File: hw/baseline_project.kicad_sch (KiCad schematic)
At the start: 20 parts, among them J101 EXT_3V3, Q101 IRLD024PBF, SW101 UP, SW102 DOWN, SW103 LEFT, SW104 RIGHT, SW105 MODE, U101 EK-TM4C123GXL, U102 ESP8266-1, U103 Adafruit ST7735R

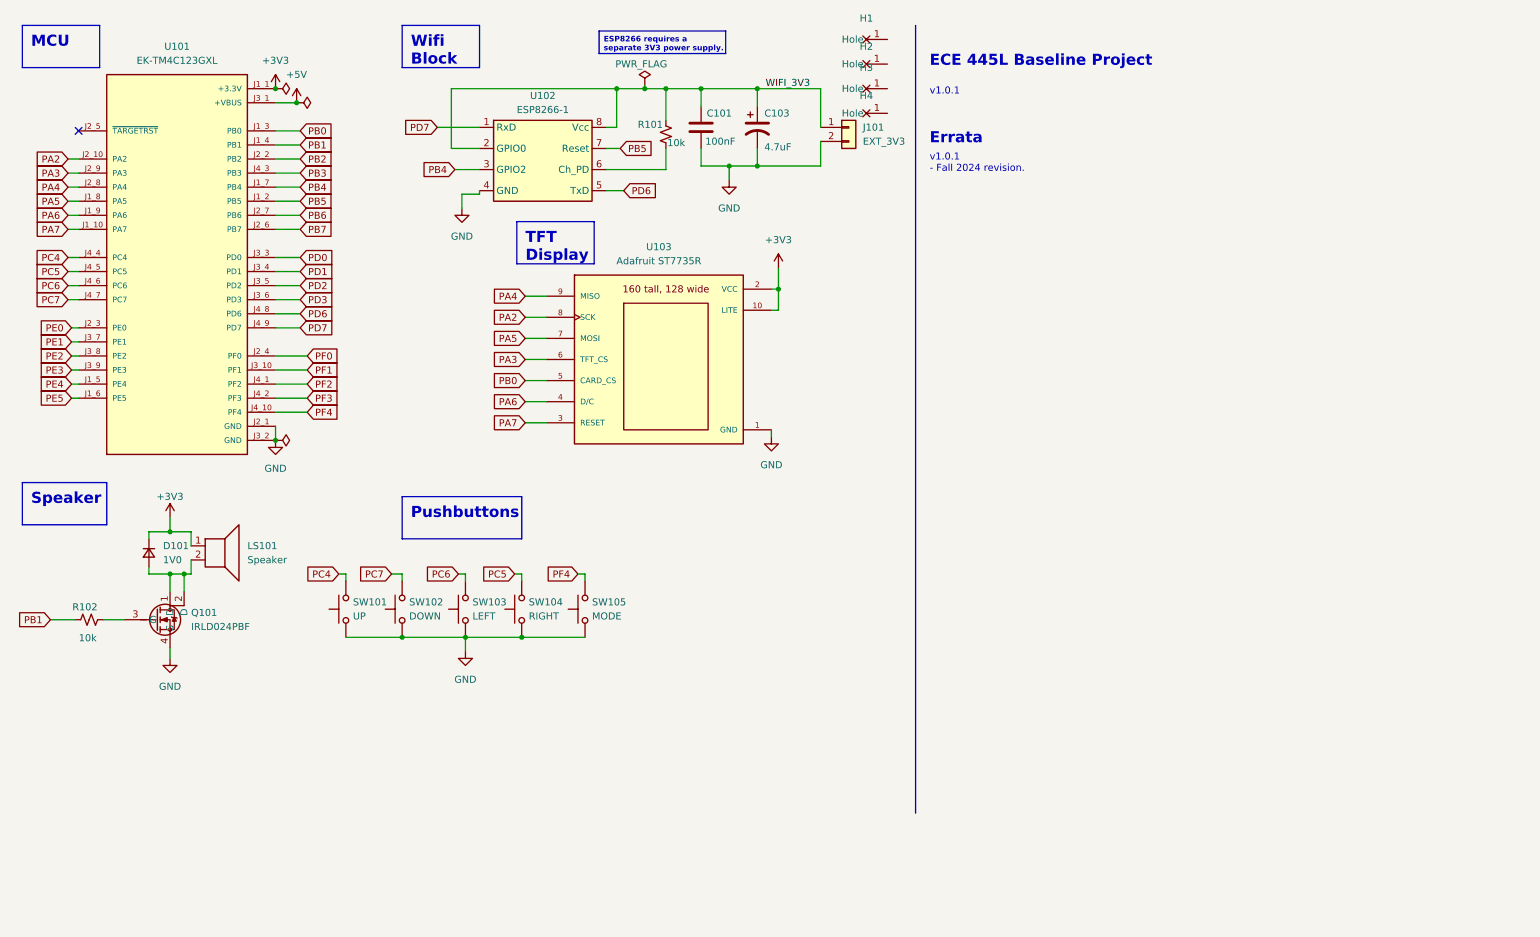
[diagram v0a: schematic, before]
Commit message: worked on actual timer funcnality
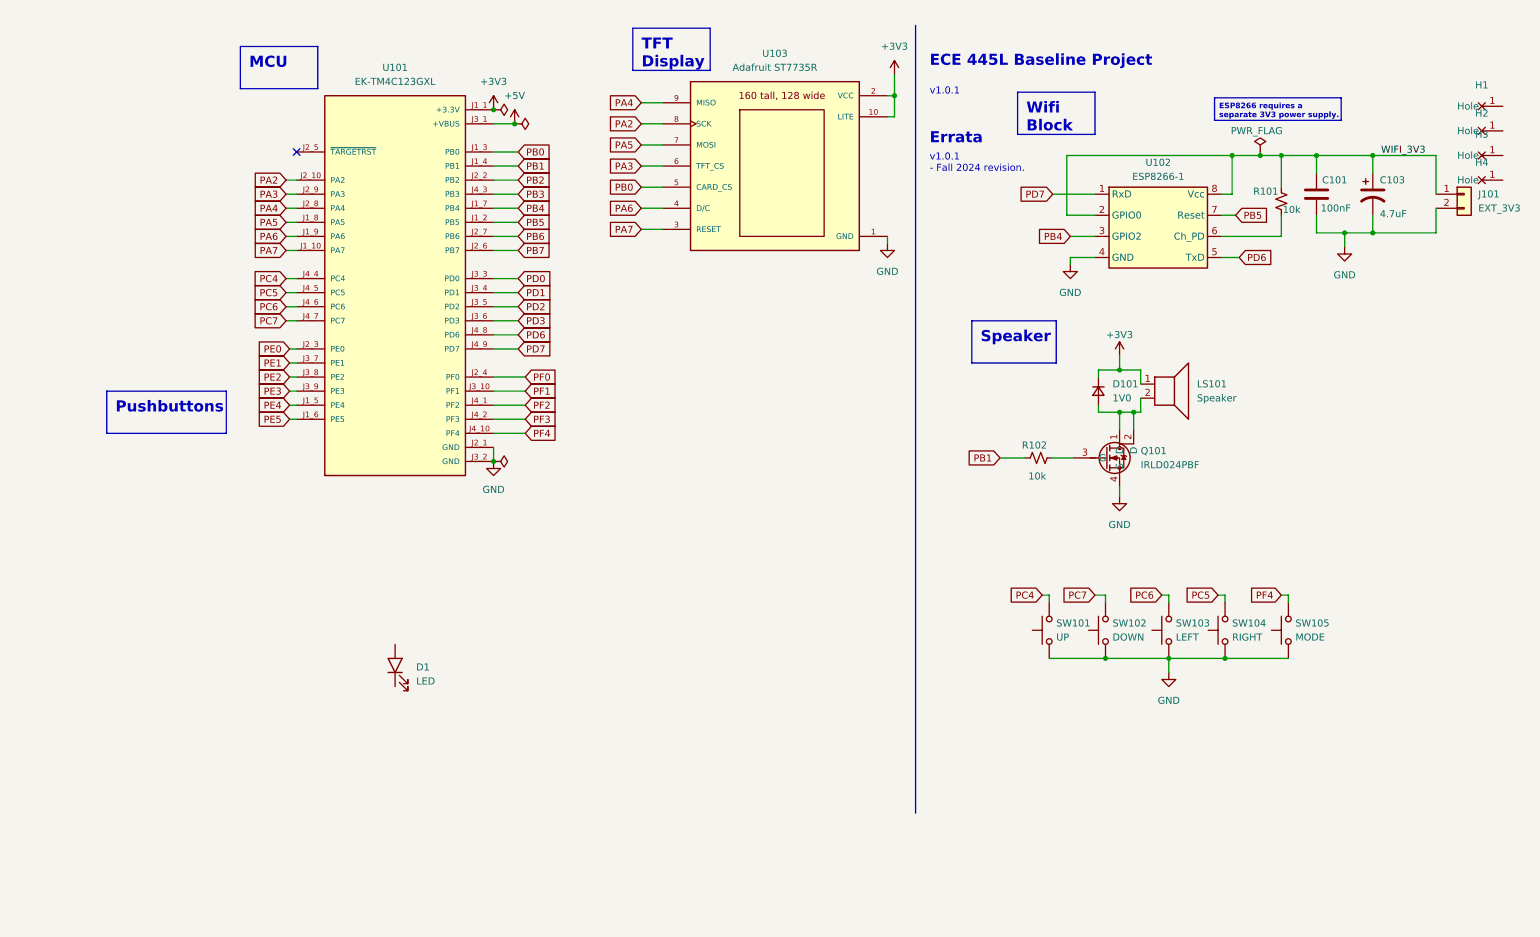
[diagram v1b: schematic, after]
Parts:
- added D1: LED, ECE445L:LED_D5.0mm, symbol ECE445L:LED
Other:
- moved on the sheet: C101, C103, D101, H1, H2, H3, H4, J101, LS101, Q101, R101, R102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

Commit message: kicad work
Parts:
- removed D1: LED, ECE445L:LED_D5.0mm, symbol ECE445L:LED
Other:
- moved on the sheet: D101, LS101, Q101, R102, SW101, SW102, SW103, SW104, SW105

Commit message: fixed the schematic to match the physical pinout
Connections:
- net PC4: no longer SW101.2
- net PC5: no longer SW104.2
- net PC6: no longer SW103.2
- net PC7: no longer SW102.2
- net PD0: now also SW101.2
- net PD1: now also SW102.2
- net PD2: now also SW103.2
- net PD3: now also SW104.2
- net PF4: no longer SW105.2
- new net PD5: SW105.2
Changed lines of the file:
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@@
 		)
 	)
-	(global_label "PC7"
+	(global_label "PD1"
 		(shape input)
 		(at 45.085 157.48 180)
@@
 		)
 	)
-	(global_label "PC4"
+	(global_label "PD0"
 		(shape input)
 		(at 35.56 157.48 180)
@@
 		)
 	)
+	(global_label "PD2"
+		(shape input)
+		(at 57.15 157.48 180)
+		(fields_autoplaced yes)
+		(effects
+			(font
+				(size 1.27 1.27)
+			)
+			(justify right)
+		)
+		(property "Intersheetrefs" "${INTERSHEET_REFS}"
+			(at 50.4153 157.48 0)
+			(effects
+				(font
+					(size 1.27 1.27)
+				)
+				(justify right)
+				(hide yes)
+			)
+		)
+	)
+	(global_label "PD0"
+		(shape input)
+		(at 104.775 60.96 0)
+		(fields_autoplaced yes)
+		(effects
+			(font
+				(size 1.27 1.27)
+			)
+			(justify left)
+		)
+		(property "Intersheetrefs" "${INTERSHEET_REFS}"
+			(at 111.5097 60.96 0)
+			(effects
+				(font
+					(size 1.27 1.27)
+				)
+				(justify left)
+				(hide yes)
+			)
+		)
+	)
+	(global_label "PB7"
+		(shape input)
+		(at 104.775 55.88 0)
+		(fields_autoplaced yes)
+		(effects
+			(font
+				(size 1.27 1.27)
+			)
+			(justify left)
+		)
+		(property "Intersheetrefs" "${INTERSHEET_REFS}"
+			(at 111.5097 55.88 0)
+			(effects
+				(font
+					(size 1.27 1.27)
+				)
+				(justify left)
+				(hide yes)
+			)
+		)
+	)
+	(global_label "PD6"
+		(shape input)
+		(at 234.95 57.15 0)
+		(fields_autoplaced yes)
+		(effects
+			(font
+				(size 1.27 1.27)
+			)
+			(justify left)
+		)
+		(property "Intersheetrefs" "${INTERSHEET_REFS}"
+			(at 241.6847 57.15 0)
+			(effects
+				(font
+					(size 1.27 1.27)
+				)
+				(justify left)
+				(hide yes)
+			)
+		)
+	)
+	(global_label "PA2"
+		(shape input)
+		(at 62.865 43.18 180)
+		(fields_autoplaced yes)
+		(effects
+			(font
+				(size 1.27 1.27)
+			)
+			(justify right)
+		)
+		(property "Intersheetrefs" "${INTERSHEET_REFS}"
+			(at 56.3117 43.18 0)
+			(effects
+				(font
+					(size 1.27 1.27)
+				)
+				(justify right)
+				(hide yes)
+			)
+		)
+	)
+	(global_label "PA7"
+		(shape input)
+		(at 127 52.07 180)
+		(fields_autoplaced yes)
+		(effects
+			(font
+				(size 1.27 1.27)
+			)
+			(justify right)
+		)
+		(property "Intersheetrefs" "${INTERSHEET_REFS}"
+			(at 120.4467 52.07 0)
+			(effects
+				(font
+					(size 1.27 1.27)
+				)
+				(justify right)
+				(hide yes)
+			)
+		)
+	)
+	(global_label "PB1"
+		(shape input)
+		(at 125.73 132.715 180)
+		(fields_autoplaced yes)
+		(effects
+			(font
+				(size 1.27 1.27)
+			)
+			(justify right)
+		)
+		(property "Intersheetrefs" "${INTERSHEET_REFS}"
+			(at 118.9953 132.715 0)
+			(effects
+				(font
+					(size 1.27 1.27)
+				)
+				(justify right)
+				(hide yes)
+			)
+		)
+	)
+	(global_label "PA6"
+		(shape input)
+		(at 127 48.26 180)
+		(fields_autoplaced yes)
+		(effects
+			(font
+				(size 1.27 1.27)
+			)
+			(justify right)
+		)
+		(property "Intersheetrefs" "${INTERSHEET_REFS}"
+			(at 120.4467 48.26 0)
+			(effects
+				(font
+					(size 1.27 1.27)
+				)
+				(justify right)
+				(hide yes)
+			)
+		)
+	)
+	(global_label "PF0"
+		(shape input)
+		(at 106.045 78.74 0)
+		(fields_autoplaced yes)
+		(effects
+			(font
+				(size 1.27 1.27)
+			)
+			(justify left)
+		)
+		(property "Intersheetrefs" "${INTERSHEET_REFS}"
+			(at 112.5983 78.74 0)
+			(effects
+				(font
+					(size 1.27 1.27)
+				)
+				(justify left)
+				(hide yes)
+			)
+		)
+	)
 	(global_label "PC6"
 		(shape input)
-		(at 57.15 157.48 180)
-		(fields_autoplaced yes)
-		(effects
-			(font
-				(size 1.27 1.27)
-			)
-			(justify right)
-		)
-		(property "Intersheetrefs" "${INTERSHEET_REFS}"
-			(at 50.4153 157.48 0)
-			(effects
-				(font
-					(size 1.27 1.27)
-				)
-				(justify right)
-				(hide yes)
-			)
-		)
-	)
-	(global_label "PD0"
-		(shape input)
-		(at 104.775 60.96 0)
-		(fields_autoplaced yes)
-		(effects
-			(font
-				(size 1.27 1.27)
-			)
-			(justify left)
-		)
-		(property "Intersheetrefs" "${INTERSHEET_REFS}"
-			(at 111.5097 60.96 0)
-			(effects
-				(font
-					(size 1.27 1.27)
-				)
-				(justify left)
-				(hide yes)
-			)
-		)
-	)
-	(global_label "PB7"
-		(shape input)
-		(at 104.775 55.88 0)
-		(fields_autoplaced yes)
-		(effects
-			(font
-				(size 1.27 1.27)
-			)
-			(justify left)
-		)
-		(property "Intersheetrefs" "${INTERSHEET_REFS}"
-			(at 111.5097 55.88 0)
-			(effects
-				(font
-					(size 1.27 1.27)
-				)
-				(justify left)
-				(hide yes)
-			)
-		)
-	)
-	(global_label "PD6"
-		(shape input)
-		(at 234.95 57.15 0)
-		(fields_autoplaced yes)
-		(effects
-			(font
-				(size 1.27 1.27)
-			)
-			(justify left)
-		)
-		(property "Intersheetrefs" "${INTERSHEET_REFS}"
-			(at 241.6847 57.15 0)
-			(effects
-				(font
-					(size 1.27 1.27)
-				)
-				(justify left)
-				(hide yes)
-			)
-		)
-	)
-	(global_label "PA2"
-		(shape input)
-		(at 62.865 43.18 180)
-		(fields_autoplaced yes)
-		(effects
-			(font
-				(size 1.27 1.27)
-			)
-			(justify right)
-		)
-		(property "Intersheetrefs" "${INTERSHEET_REFS}"
-			(at 56.3117 43.18 0)
-			(effects
-				(font
-					(size 1.27 1.27)
-				)
-				(justify right)
-				(hide yes)
-			)
-		)
-	)
-	(global_label "PA7"
-		(shape input)
-		(at 127 52.07 180)
-		(fields_autoplaced yes)
-		(effects
-			(font
-				(size 1.27 1.27)
-			)
-			(justify right)
-		)
-		(property "Intersheetrefs" "${INTERSHEET_REFS}"
-			(at 120.4467 52.07 0)
-			(effects
-				(font
-					(size 1.27 1.27)
-				)
-				(justify right)
-				(hide yes)
-			)
-		)
-	)
-	(global_label "PB1"
-		(shape input)
-		(at 125.73 132.715 180)
-		(fields_autoplaced yes)
-		(effects
-			(font
-				(size 1.27 1.27)
-			)
-			(justify right)
-		)
-		(property "Intersheetrefs" "${INTERSHEET_REFS}"
-			(at 118.9953 132.715 0)
-			(effects
-				(font
-					(size 1.27 1.27)
-				)
-				(justify right)
-				(hide yes)
-			)
-		)
-	)
-	(global_label "PA6"
-		(shape input)
-		(at 127 48.26 180)
-		(fields_autoplaced yes)
-		(effects
-			(font
-				(size 1.27 1.27)
-			)
-			(justify right)
-		)
-		(property "Intersheetrefs" "${INTERSHEET_REFS}"
-			(at 120.4467 48.26 0)
-			(effects
-				(font
-					(size 1.27 1.27)
-				)
-				(justify right)
-				(hide yes)
-			)
-		)
-	)
-	(global_label "PF0"
-		(shape input)
-		(at 106.045 78.74 0)
-		(fields_autoplaced yes)
-		(effects
-			(font
-				(size 1.27 1.27)
-			)
-			(justify left)
-		)
-		(property "Intersheetrefs" "${INTERSHEET_REFS}"
-			(at 112.5983 78.74 0)
-			(effects
-				(font
-					(size 1.27 1.27)
-				)
-				(justify left)
-				(hide yes)
-			)
-		)
-	)
-	(global_label "PC6"
-		(shape input)
 		(at 62.865 66.04 180)
 		(fields_autoplaced yes)
@@
 		)
 	)
-	(global_label "PC5"
+	(global_label "PD3"
 		(shape input)
 		(at 67.31 157.48 180)
@@
 		)
 	)
-	(global_label "PF4"
+	(global_label "PD5"
 		(shape input)
 		(at 78.74 157.48 180)
@@
 		)
 		(property "Intersheetrefs" "${INTERSHEET_REFS}"
-			(at 72.1867 157.48 0)
-			(effects
-				(font
+			(at 72.0053 157.48 0)
+			(effects
+				(font
